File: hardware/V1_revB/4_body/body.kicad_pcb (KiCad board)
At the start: 2 copper layers, 57.8 x 40.6 mm, 36 parts, among them J8 , SW4 SK14EG13, U1 STP08CP05XT

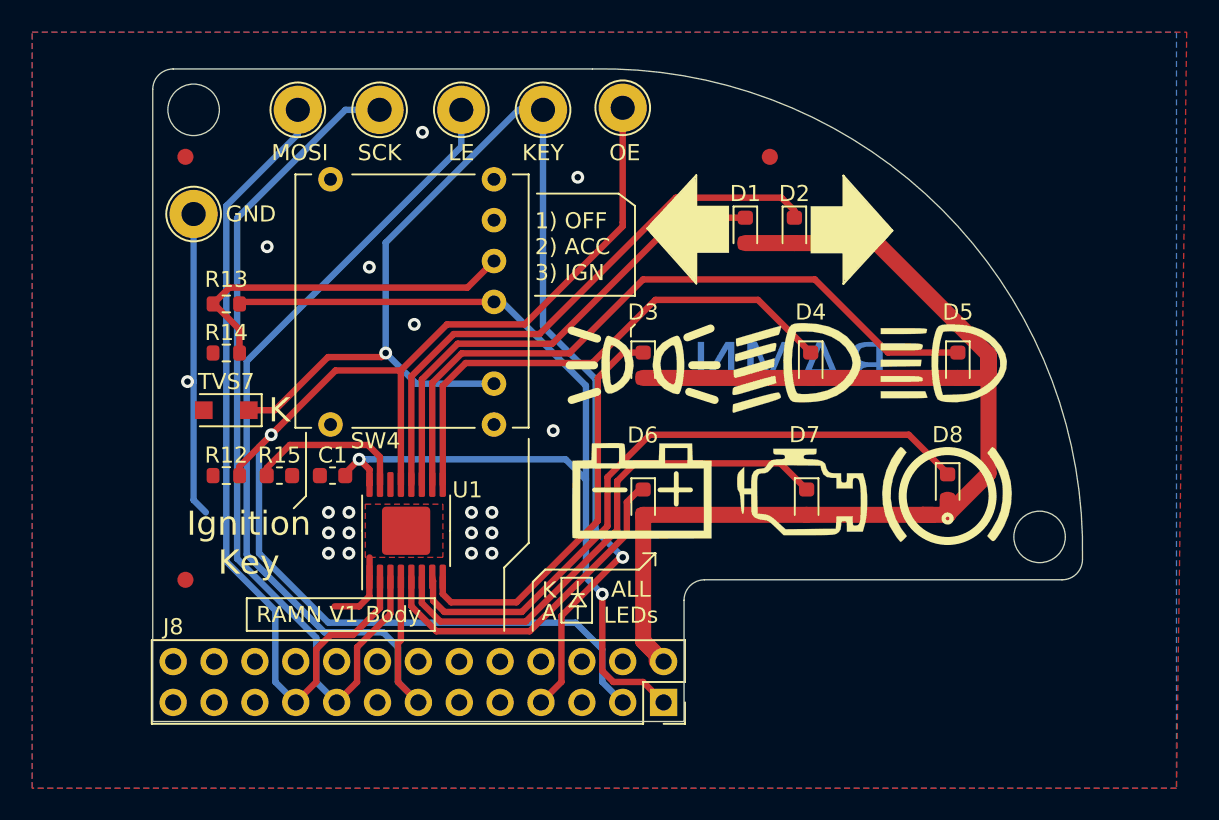
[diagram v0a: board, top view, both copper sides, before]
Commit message: feat: test points in body got changed
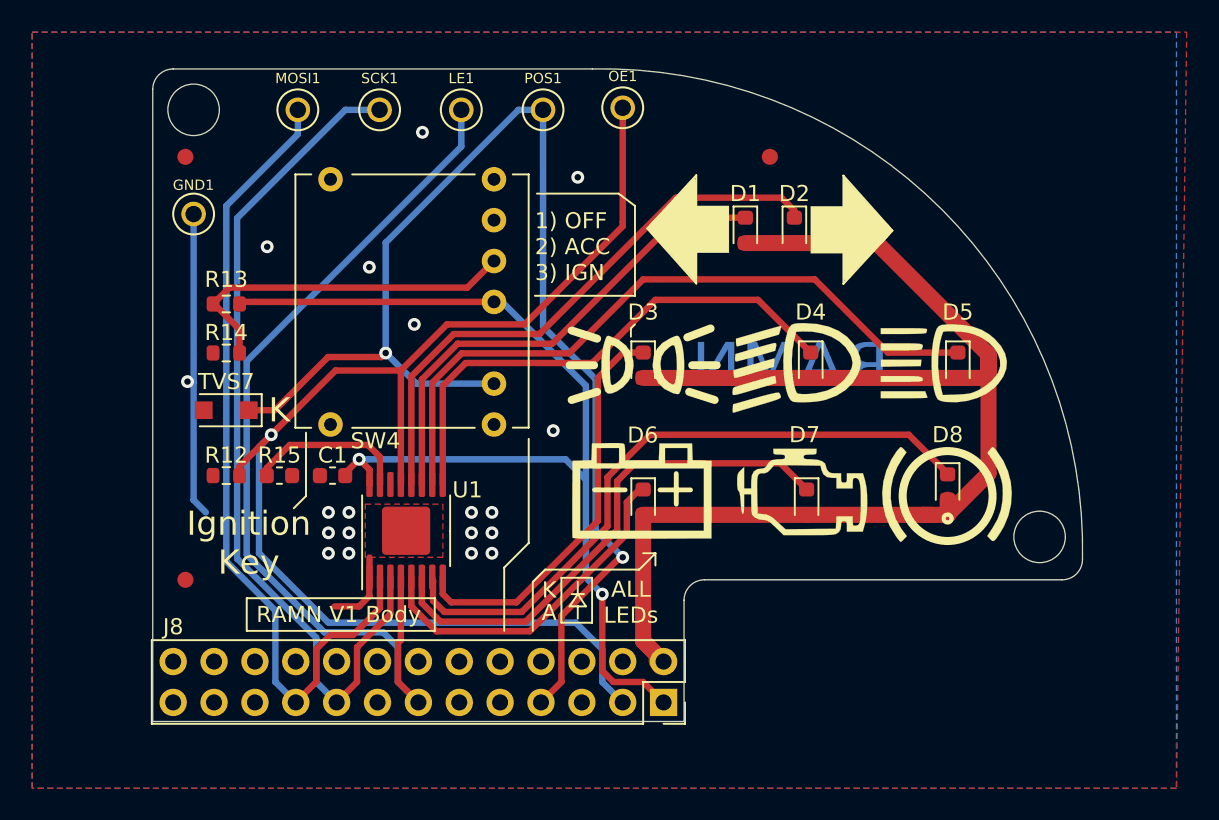
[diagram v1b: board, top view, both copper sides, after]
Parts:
- GND1: renamed from GND; footprint TestPoint:TestPoint_Loop_D2.54mm_Drill1.5mm_Beaded -> Global_Library:KEYSTONE_5002
- J8: value (none) -> ~
- LE1: renamed from LE; footprint TestPoint:TestPoint_Loop_D2.54mm_Drill1.5mm_Beaded -> Global_Library:KEYSTONE_5002
- MOSI1: renamed from MOSI; footprint TestPoint:TestPoint_Loop_D2.54mm_Drill1.5mm_Beaded -> Global_Library:KEYSTONE_5002
- OE1: renamed from OE; footprint TestPoint:TestPoint_Loop_D2.54mm_Drill1.5mm_Beaded -> Global_Library:KEYSTONE_5002
- POS1: renamed from KEY; footprint TestPoint:TestPoint_Loop_D2.54mm_Drill1.5mm_Beaded -> Global_Library:KEYSTONE_5002
- SCK1: renamed from SCK; footprint TestPoint:TestPoint_Loop_D2.54mm_Drill1.5mm_Beaded -> Global_Library:KEYSTONE_5002
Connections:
- J8 pad 10: Net-(J8-Pad10) -> unconnected-(J8-Pin_10-Pad10)
- J8 pad 11: Net-(J8-Pad11) -> unconnected-(J8-Pin_11-Pad11)
- J8 pad 12: Net-(J8-Pad12) -> unconnected-(J8-Pin_12-Pad12)
- J8 pad 14: Net-(J8-Pad14) -> unconnected-(J8-Pin_14-Pad14)
- J8 pad 15: Net-(J8-Pad15) -> unconnected-(J8-Pin_15-Pad15)
- J8 pad 16: Net-(J8-Pad16) -> unconnected-(J8-Pin_16-Pad16)
- J8 pad 18: Net-(J8-Pad18) -> unconnected-(J8-Pin_18-Pad18)
- J8 pad 20: Net-(J8-Pad20) -> unconnected-(J8-Pin_20-Pad20)
- J8 pad 21: Net-(J8-Pad21) -> unconnected-(J8-Pin_21-Pad21)
- J8 pad 22: Net-(J8-Pad22) -> unconnected-(J8-Pin_22-Pad22)
- J8 pad 23: Net-(J8-Pad23) -> unconnected-(J8-Pin_23-Pad23)
- J8 pad 24: Net-(J8-Pad24) -> unconnected-(J8-Pin_24-Pad24)
- J8 pad 25: Net-(J8-Pad25) -> unconnected-(J8-Pin_25-Pad25)
- J8 pad 26: Net-(J8-Pad26) -> unconnected-(J8-Pin_26-Pad26)
- J8 pad 5: Net-(J8-Pad5) -> unconnected-(J8-Pin_5-Pad5)
- J8 pad 6: Net-(J8-Pad6) -> unconnected-(J8-Pin_6-Pad6)
- J8 pad 8: Net-(J8-Pad8) -> unconnected-(J8-Pin_8-Pad8)
- J8 pad 9: Net-(J8-Pad9) -> unconnected-(J8-Pin_9-Pad9)
- U1 pad 14: Net-(U1-Pad14) -> unconnected-(U1-SDO-Pad14)
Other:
- net class +5V removed
- net class Default removed
